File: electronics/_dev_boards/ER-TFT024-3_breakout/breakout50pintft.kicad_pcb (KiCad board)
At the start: 2 copper layers, 8 parts, among them J1 CONN_02X15, Q1 Q_PMOS_GSD, U1 ER-TFT024-3

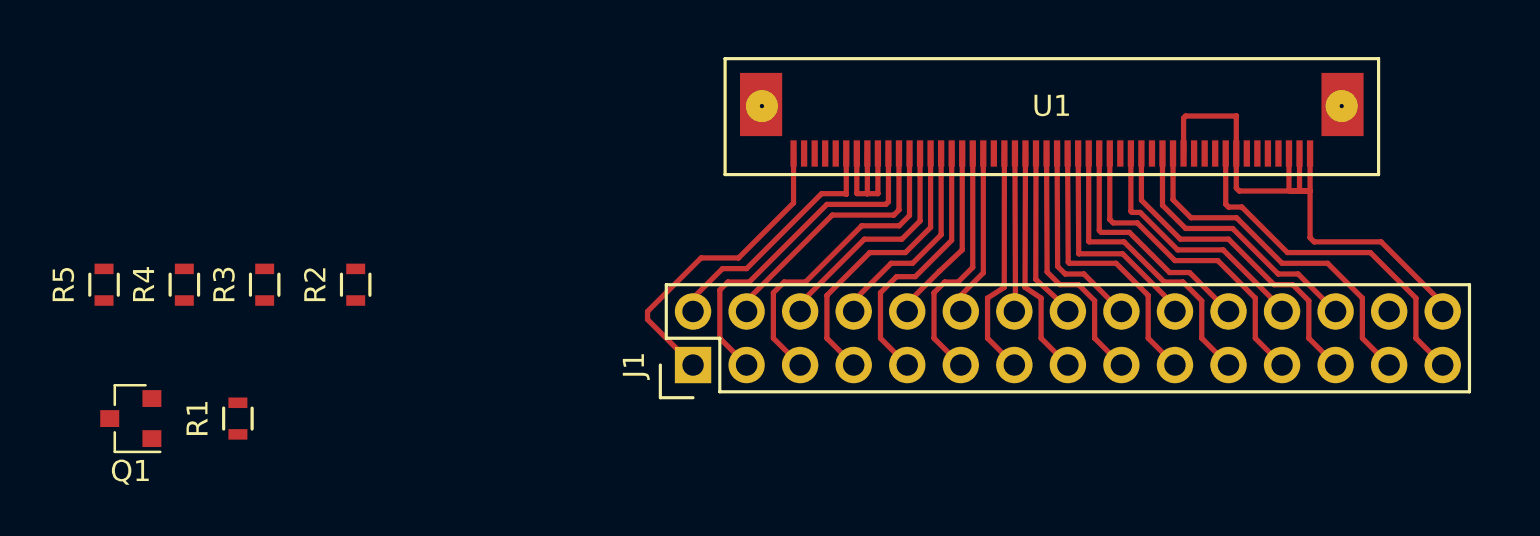
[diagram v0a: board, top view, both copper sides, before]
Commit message: Finishg routing tft breakout, including outline
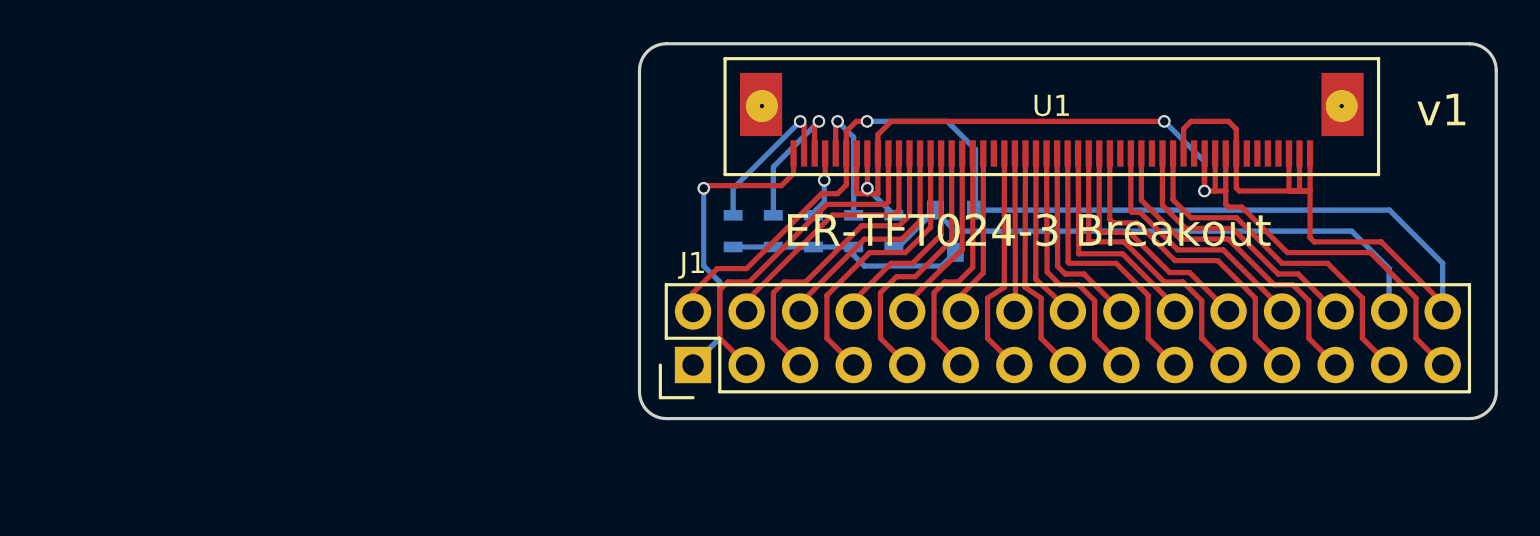
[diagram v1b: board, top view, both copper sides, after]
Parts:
- Q1, R1, R2, R3, R4, R5: moved to B.Cu
- moved Q1 40.1 mm to (166.1, 109.2), turned to 270 degrees
- moved R1 32.4 mm to (163.2, 109.2)
- moved R5 30.0 mm to (155.6, 109.2)
- moved R4 28.1 mm to (157.5, 109.2)
- moved R3 26.2 mm to (159.4, 109.2)
- moved R2 23.8 mm to (161.3, 109.2)
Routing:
- net GND: track 40.1 -> 76.0 mm, vias 0 -> 1
- net BL: track 0.00 -> 27.4 mm
- net +3V3: track 23.7 -> 48.9 mm, vias 0 -> 3
- net Net-(Q1-Pad3): track 0.00 -> 11.4 mm
- net Net-(R5-Pad2): track 0.00 -> 7.37 mm, vias 0 -> 1
- net Net-(R4-Pad2): track 0.00 -> 6.96 mm, vias 0 -> 1
- net Net-(R2-Pad2): track 0.00 -> 6.33 mm, vias 0 -> 1
- net Net-(R3-Pad2): track 0.00 -> 3.16 mm, vias 0 -> 1
- net +5V: track 14.8 -> 14.7 mm, vias 0 -> 1
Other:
- board outline added: 40.6 x 17.8 mm
- board text added: "ER-TFT024-3 Breakout"
- board text added: "v1"

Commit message: Swap to HandSoldering versions on tft breakout
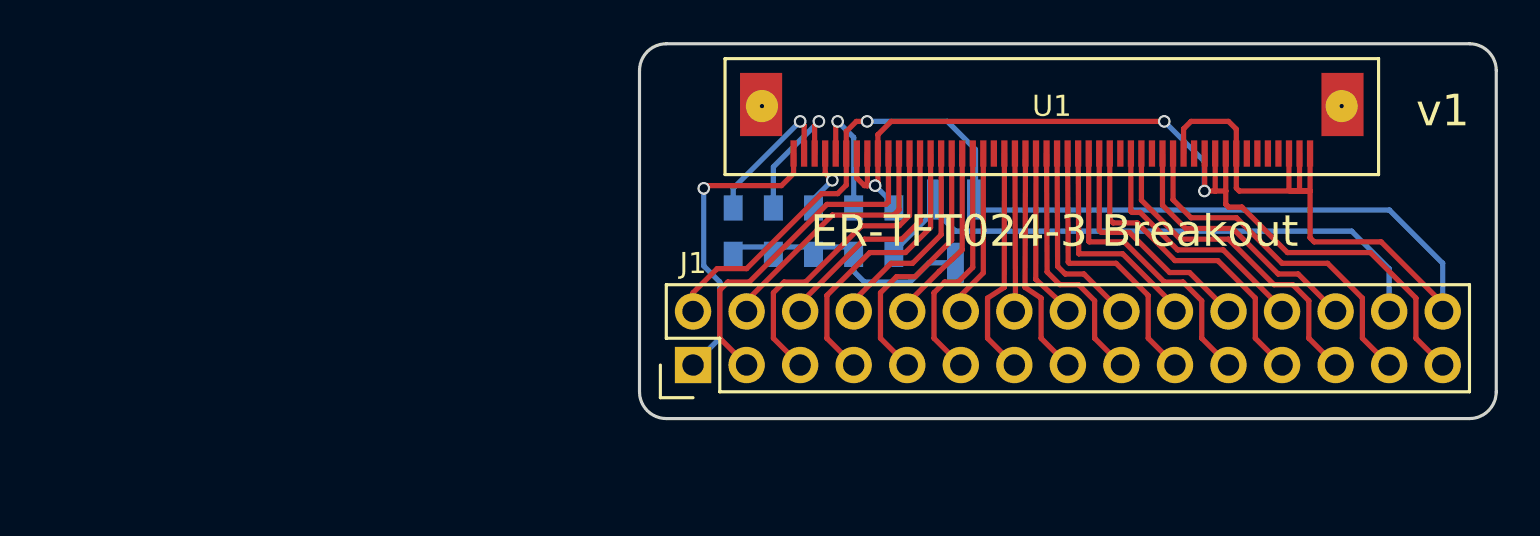
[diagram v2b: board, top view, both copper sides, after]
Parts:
- Q1: footprint TO_SOT_Packages_SMD:SOT-23 -> TO_SOT_Packages_SMD:SOT-23_Handsoldering
- R1, R2, R3, R4, R5: footprint Resistors_SMD:R_0603 -> Resistors_SMD:R_0603_HandSoldering
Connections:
- U1 pad 20: Net-(U1-Pad20) -> (no net)
- U1 pad 32: Net-(U1-Pad32) -> (no net)
- U1 pad 35: Net-(U1-Pad35) -> (no net)
- U1 pad 39: Net-(U1-Pad39) -> (no net)
- U1 pad 44: Net-(U1-Pad44) -> (no net)
- U1 pad 45: Net-(U1-Pad45) -> (no net)
- U1 pad 46: Net-(U1-Pad46) -> (no net)
- U1 pad 47: Net-(U1-Pad47) -> (no net)
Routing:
- net +3V3: track 48.9 -> 47.1 mm
- net Net-(Q1-Pad3): track 11.4 -> 12.3 mm
